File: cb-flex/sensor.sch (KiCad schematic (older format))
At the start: 18 parts, among them P4 CONN_01X04, Q1 Q_NMOS_GSD, Q2 Q_NMOS_GSD, U1 BMP180, U3 SI7021, U4 TSL2561

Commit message: Finishing layout
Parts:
- added C29, C32: 100n, mysmd:SM0603S, symbol C
- added C31: 1u, mysmd:SM0603S, symbol C
- added U10: MMA8652FC, mysmd:DFN-10, symbol MMA8652FC
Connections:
- net GND: now also C29.2, C31.2, C32.2, U10.6 (GND), U10.7 (GND), U10.9 (GND)
- net SCL: now also U10.2 (SCL)
- net SDA: now also U10.10 (SDA)
- new net: C29.1, U10.4 (BYP)
- new net ACC_INT1: U10.3 (INT1)
- new net ACC_INT2: U10.5 (INT2)
- new net EN_ACC: C31.1, C32.1, U10.1 (VDD), U10.8 (VDDIO)
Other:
- note added: "3-axis acceleration sensor"
- moved on the sheet: C2, C24, C3, C7, P4, Q1, Q2, R1, R13, R2, R3, R6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

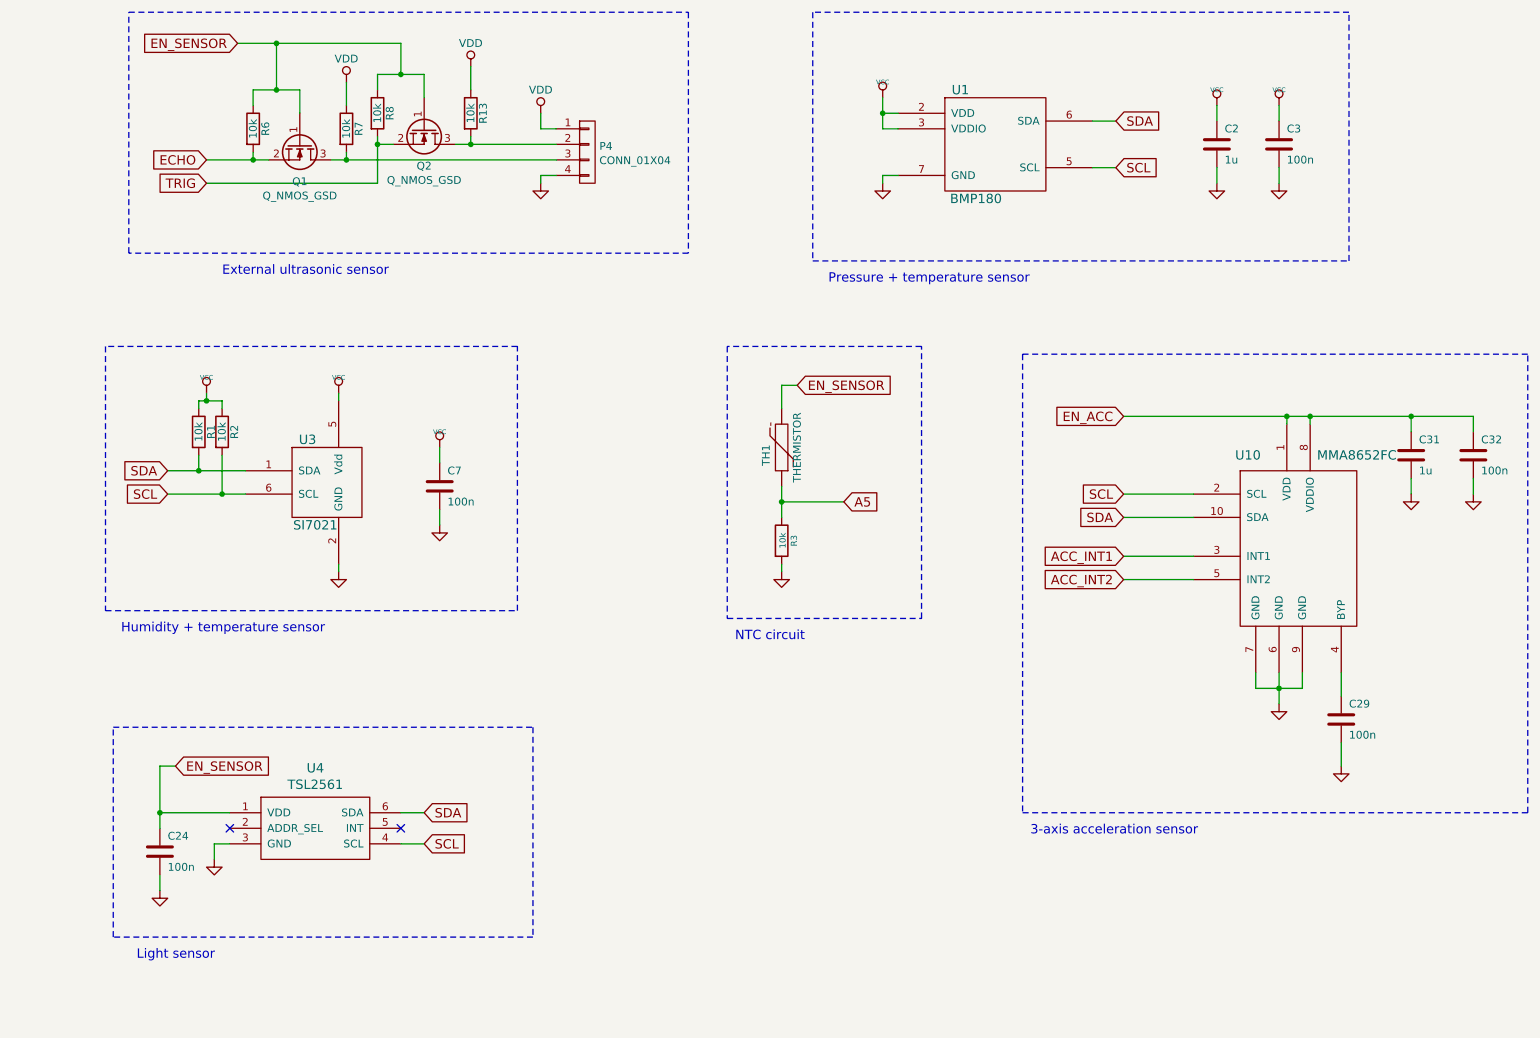
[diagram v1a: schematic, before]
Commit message: PCB layour finished
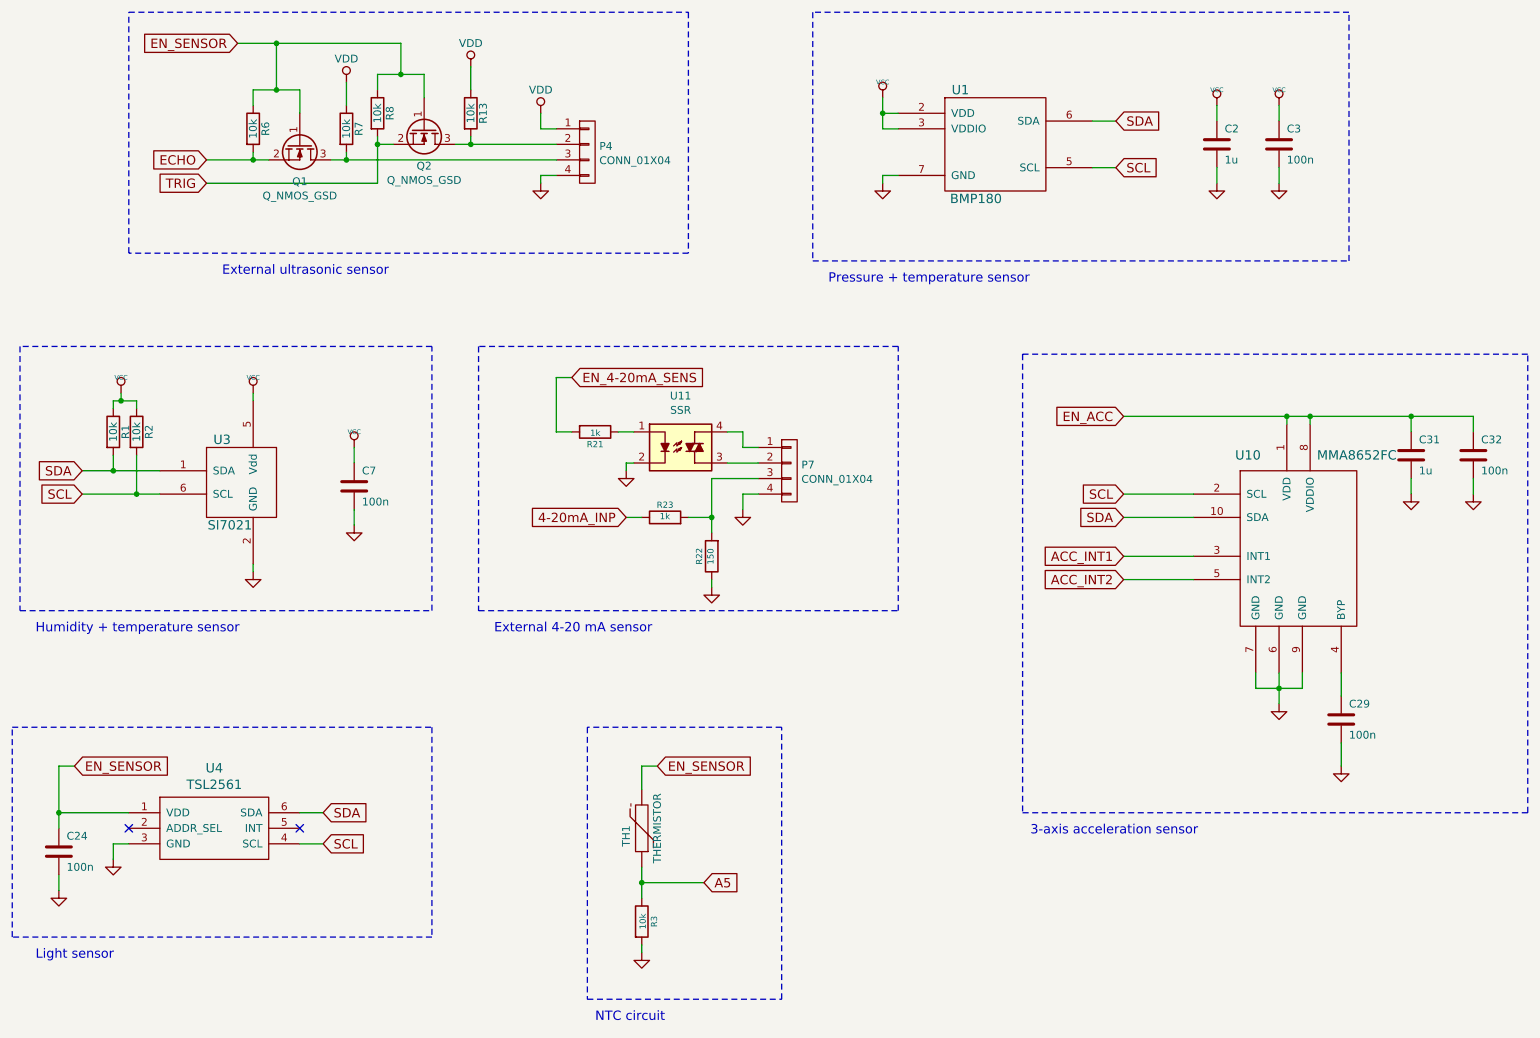
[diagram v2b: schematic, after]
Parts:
- added P7: CONN_01X04, Pin_Headers:Pin_Header_Straight_1x04, symbol CONN_01X04
- added R21, R23: 1k, mysmd:SM0603S, symbol R
- added R22: 150, mysmd:SM0603S, symbol R
- added U11: SSR, mysmd:SMT-DIP-4, symbol FODM3053
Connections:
- net GND: now also P7.4 (P4), R22.1, U11.2
- new net: R21.1, U11.1
- new net: P7.2 (P2), U11.3
- new net: P7.1 (P1), U11.4
- new net: P7.3 (P3), R22.2, R23.2
- new net 4-20mA_INP: R23.1
- new net EN_4-20mA_SENS: R21.2
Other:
- note added: "External 4-20 mA sensor"
- moved on the sheet: C24, C7, R1, R2, R3, TH1, U3, U4

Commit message: PCB layout finished
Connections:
- net VEXT: now reaches P7.1 (P1), U11.4
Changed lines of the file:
@@
 $EndComp
 $Comp
-L GND #PWR62
+L GND #PWR055
 U 1 1 56BDE154
 P 3000 4150
-F 0 "#PWR62" H 3000 4150 30  0001 C CNN
+F 0 "#PWR055" H 3000 4150 30  0001 C CNN
 F 1 "GND" H 3000 4080 30  0001 C CNN
 F 2 "" H 3000 4150 60  0001 C CNN
@@
 $EndComp
 $Comp
-L GND #PWR59
+L GND #PWR056
 U 1 1 56BDE161
 P 2350 4450
-F 0 "#PWR59" H 2350 4450 30  0001 C CNN
+F 0 "#PWR056" H 2350 4450 30  0001 C CNN
 F 1 "GND" H 2350 4380 30  0001 C CNN
 F 2 "" H 2350 4450 60  0001 C CNN
@@
 $EndComp
 $Comp
-L VCC #PWR57
+L VCC #PWR057
 U 1 1 56BDE177
 P 1500 3300
-F 0 "#PWR57" H 1500 3400 30  0001 C CNN
+F 0 "#PWR057" H 1500 3400 30  0001 C CNN
 F 1 "VCC" H 1500 3400 30  0000 C CNN
 F 2 "" H 1500 3300 60  0000 C CNN
@@
 $EndComp
 $Comp
-L VCC #PWR58
+L VCC #PWR058
 U 1 1 56BDE17D
 P 2350 3300
-F 0 "#PWR58" H 2350 3400 30  0001 C CNN
+F 0 "#PWR058" H 2350 3400 30  0001 C CNN
 F 1 "VCC" H 2350 3400 30  0000 C CNN
 F 2 "" H 2350 3300 60  0000 C CNN
@@
 $EndComp
 $Comp
-L VCC #PWR61
+L VCC #PWR059
 U 1 1 56BDE183
 P 3000 3650
-F 0 "#PWR61" H 3000 3750 30  0001 C CNN
+F 0 "#PWR059" H 3000 3750 30  0001 C CNN
 F 1 "VCC" H 3000 3750 30  0000 C CNN
 F 2 "" H 3000 3650 60  0000 C CNN
@@
 $EndComp
 $Comp
-L GND #PWR73
+L GND #PWR060
 U 1 1 56BDE190
 P 8550 1950
-F 0 "#PWR73" H 8550 1950 30  0001 C CNN
+F 0 "#PWR060" H 8550 1950 30  0001 C CNN
 F 1 "GND" H 8550 1880 30  0001 C CNN
 F 2 "" H 8550 1950 60  0001 C CNN
@@
 $EndComp
 $Comp
-L GND #PWR75
+L GND #PWR061
 U 1 1 56BDE19D
 P 8950 1950
-F 0 "#PWR75" H 8950 1950 30  0001 C CNN
+F 0 "#PWR061" H 8950 1950 30  0001 C CNN
 F 1 "GND" H 8950 1880 30  0001 C CNN
 F 2 "" H 8950 1950 60  0001 C CNN
@@
 $EndComp
 $Comp
-L VCC #PWR72
+L VCC #PWR062
 U 1 1 56BDE1A3
 P 8550 1450
-F 0 "#PWR72" H 8550 1550 30  0001 C CNN
+F 0 "#PWR062" H 8550 1550 30  0001 C CNN
 F 1 "VCC" H 8550 1550 30  0000 C CNN
 F 2 "" H 8550 1450 60  0001 C CNN
@@
 $EndComp
 $Comp
-L VCC #PWR74
+L VCC #PWR063
 U 1 1 56BDE1A9
 P 8950 1450
-F 0 "#PWR74" H 8950 1550 30  0001 C CNN
+F 0 "#PWR063" H 8950 1550 30  0001 C CNN
 F 1 "VCC" H 8950 1550 30  0000 C CNN
 F 2 "" H 8950 1450 60  0001 C CNN
@@
 $EndComp
 $Comp
-L VCC #PWR70
+L VCC #PWR064
 U 1 1 56BDE1B6
 P 6400 1400
-F 0 "#PWR70" H 6400 1500 30  0001 C CNN
+F 0 "#PWR064" H 6400 1500 30  0001 C CNN
 F 1 "VCC" H 6400 1500 30  0000 C CNN
 F 2 "" H 6400 1400 60  0001 C CNN
@@
 $EndComp
 $Comp
-L GND #PWR71
+L GND #PWR065
 U 1 1 56BDE1BC
 P 6400 1950
-F 0 "#PWR71" H 6400 1950 30  0001 C CNN
+F 0 "#PWR065" H 6400 1950 30  0001 C CNN
 F 1 "GND" H 6400 1880 30  0001 C CNN
 F 2 "" H 6400 1950 60  0001 C CNN
@@
 $EndComp
 $Comp
-L VDD #PWR64
+L VDD #PWR066
 U 1 1 56BDE1CB
 P 4200 1500
-F 0 "#PWR64" H 4200 1350 50  0001 C CNN
+F 0 "#PWR066" H 4200 1350 50  0001 C CNN
 F 1 "VDD" H 4200 1650 50  0000 C CNN
 F 2 "" H 4200 1500 60  0000 C CNN
@@
 $EndComp
 $Comp
-L GND #PWR65
+L GND #PWR067
 U 1 1 56BDE1D1
 P 4200 1950
-F 0 "#PWR65" H 4200 1950 30  0001 C CNN
+F 0 "#PWR067" H 4200 1950 30  0001 C CNN
 F 1 "GND" H 4200 1880 30  0001 C CNN
 F 2 "" H 4200 1950 60  0001 C CNN
@@
 $EndComp
 $Comp
-L VDD #PWR63
+L VDD #PWR068
 U 1 1 56BDE1EE
 P 3750 1200
-F 0 "#PWR63" H 3750 1050 50  0001 C CNN
+F 0 "#PWR068" H 3750 1050 50  0001 C CNN
 F 1 "VDD" H 3750 1350 50  0000 C CNN
 F 2 "" H 3750 1200 60  0000 C CNN
@@
 $EndComp
 $Comp
-L VDD #PWR60
+L VDD #PWR069
 U 1 1 56BDE20F
 P 2950 1300
-F 0 "#PWR60" H 2950 1150 50  0001 C CNN
+F 0 "#PWR069" H 2950 1150 50  0001 C CNN
 F 1 "VDD" H 2950 1450 50  0000 C CNN
 F 2 "" H 2950 1300 60  0000 C CNN
@@
 $EndComp
 $Comp
-L GND #PWR67
+L GND #PWR070
 U 1 1 56BDE22B
 P 4850 6900
-F 0 "#PWR67" H 4850 6900 30  0001 C CNN
+F 0 "#PWR070" H 4850 6900 30  0001 C CNN
 F 1 "GND" H 4850 6830 30  0001 C CNN
 F 2 "" H 4850 6900 60  0001 C CNN
@@
 	1100 6000 1550 6000
 $Comp
-L GND #PWR56
+L GND #PWR071
 U 1 1 56BE072C
 P 1450 6300
-F 0 "#PWR56" H 1450 6300 30  0001 C CNN
+F 0 "#PWR071" H 1450 6300 30  0001 C CNN
 F 1 "GND" H 1450 6230 30  0001 C CNN
 F 2 "" H 1450 6300 60  0001 C CNN
@@
 $EndComp
 $Comp
-L GND #PWR55
+L GND #PWR072
 U 1 1 56BE0742
 P 1100 6500
-F 0 "#PWR55" H 1100 6500 30  0001 C CNN
+F 0 "#PWR072" H 1100 6500 30  0001 C CNN
 F 1 "GND" H 1100 6430 30  0001 C CNN
 F 2 "" H 1100 6500 60  0001 C CNN
@@
 $EndComp
 $Comp
-L GND #PWR76
+L GND #PWR073
 U 1 1 56BFC7BF
 P 8950 5300
-F 0 "#PWR76" H 8950 5300 30  0001 C CNN
+F 0 "#PWR073" H 8950 5300 30  0001 C CNN
 F 1 "GND" H 8950 5230 30  0001 C CNN
 F 2 "" H 8950 5300 60  0001 C CNN
@@
 	9350 5100 9350 5250
 $Comp
-L GND #PWR77
+L GND #PWR074
 U 1 1 56BFC7D2
 P 9350 5700
-F 0 "#PWR77" H 9350 5700 30  0001 C CNN
+F 0 "#PWR074" H 9350 5700 30  0001 C CNN
 F 1 "GND" H 9350 5630 30  0001 C CNN
 F 2 "" H 9350 5700 60  0001 C CNN
@@
 $EndComp
 $Comp
-L GND #PWR78
+L GND #PWR075
 U 1 1 56BFC7E0
 P 9800 3950
-F 0 "#PWR78" H 9800 3950 30  0001 C CNN
+F 0 "#PWR075" H 9800 3950 30  0001 C CNN
 F 1 "GND" H 9800 3880 30  0001 C CNN
 F 2 "" H 9800 3950 60  0001 C CNN
@@
 $EndComp
 $Comp
-L GND #PWR79
+L GND #PWR076
 U 1 1 56BFC7EF
 P 10200 3950
-F 0 "#PWR79" H 10200 3950 30  0001 C CNN
+F 0 "#PWR076" H 10200 3950 30  0001 C CNN
 F 1 "GND" H 10200 3880 30  0001 C CNN
 F 2 "" H 10200 3950 60  0001 C CNN
@@
 	4800 3550 4700 3550
 $Comp
-L GND #PWR66
+L GND #PWR077
 U 1 1 56C361B0
 P 4750 3800
-F 0 "#PWR66" H 4750 3800 30  0001 C CNN
+F 0 "#PWR077" H 4750 3800 30  0001 C CNN
 F 1 "GND" H 4750 3730 30  0001 C CNN
 F 2 "" H 4750 3800 60  0001 C CNN
@@
 	5400 3750 5600 3750
 $Comp
-L GND #PWR69
+L GND #PWR078
 U 1 1 56C36667
 P 5500 4050
-F 0 "#PWR69" H 5500 4050 30  0001 C CNN
+F 0 "#PWR078" H 5500 4050 30  0001 C CNN
 F 1 "GND" H 5500 3980 30  0001 C CNN
 F 2 "" H 5500 4050 60  0001 C CNN
@@
 	5300 4100 5150 4100
 Wire Wire Line
-	5600 3650 5500 3650
-Wire Wire Line
-	5500 3650 5500 3550
+	5500 3650 5600 3650
+Wire Wire Line
+	5500 3250 5500 3650
 Wire Wire Line
 	5500 3550 5400 3550
@@
 Connection ~ 5300 4100
 $Comp
-L GND #PWR68
+L GND #PWR079
 U 1 1 56C38E17
 P 5300 4550
-F 0 "#PWR68" H 5300 4550 30  0001 C CNN
+F 0 "#PWR079" H 5300 4550 30  0001 C CNN
 F 1 "GND" H 5300 4480 30  0001 C CNN
 F 2 "" H 5300 4550 60  0001 C CNN
@@
 Text Notes 3900 4850 0    60   ~ 0
 External 4-20 mA sensor
+Text GLabel 5650 3250 2    60   Input ~ 0
+VEXT
+Wire Wire Line
+	5500 3250 5650 3250
+Connection ~ 5500 3550
 $EndSCHEMATC
